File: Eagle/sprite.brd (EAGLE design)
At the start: 35 x 35 mm, 39 parts

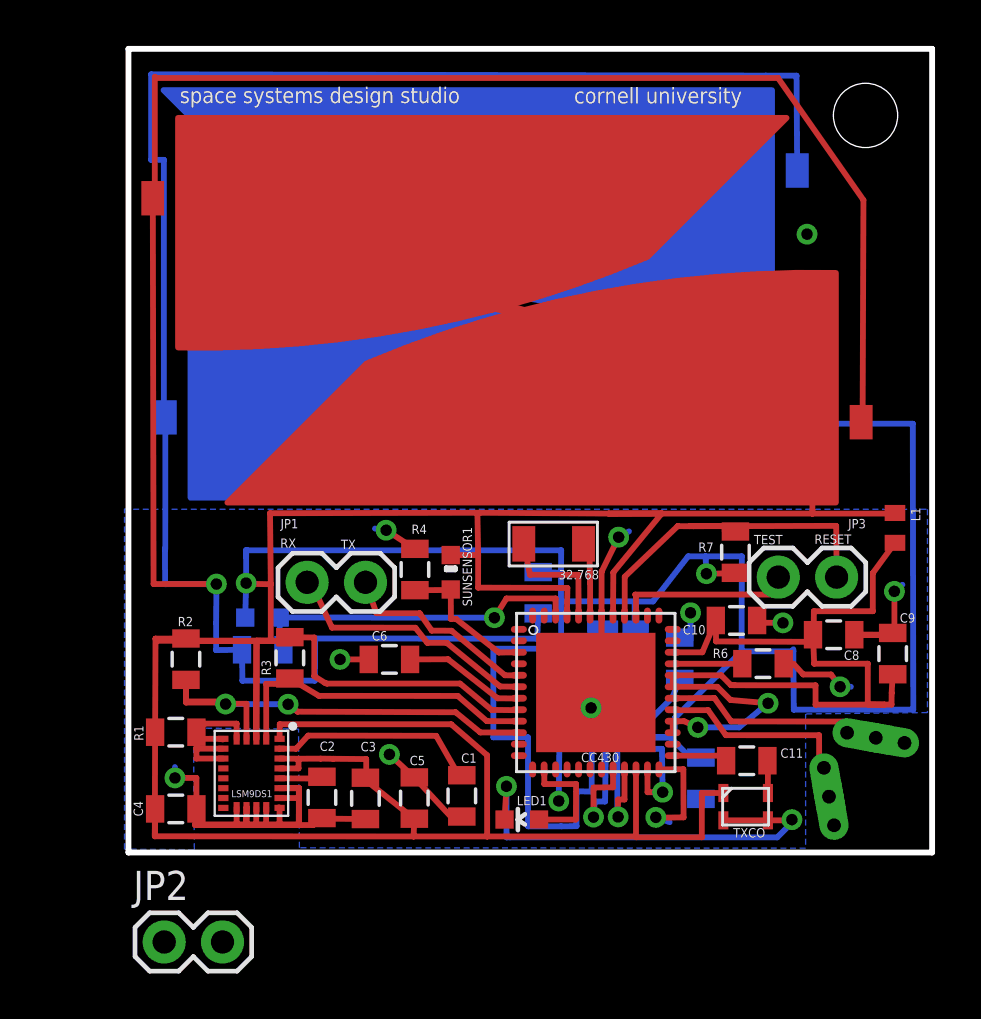
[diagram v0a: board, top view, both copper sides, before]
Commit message: Resized, still needs spacers
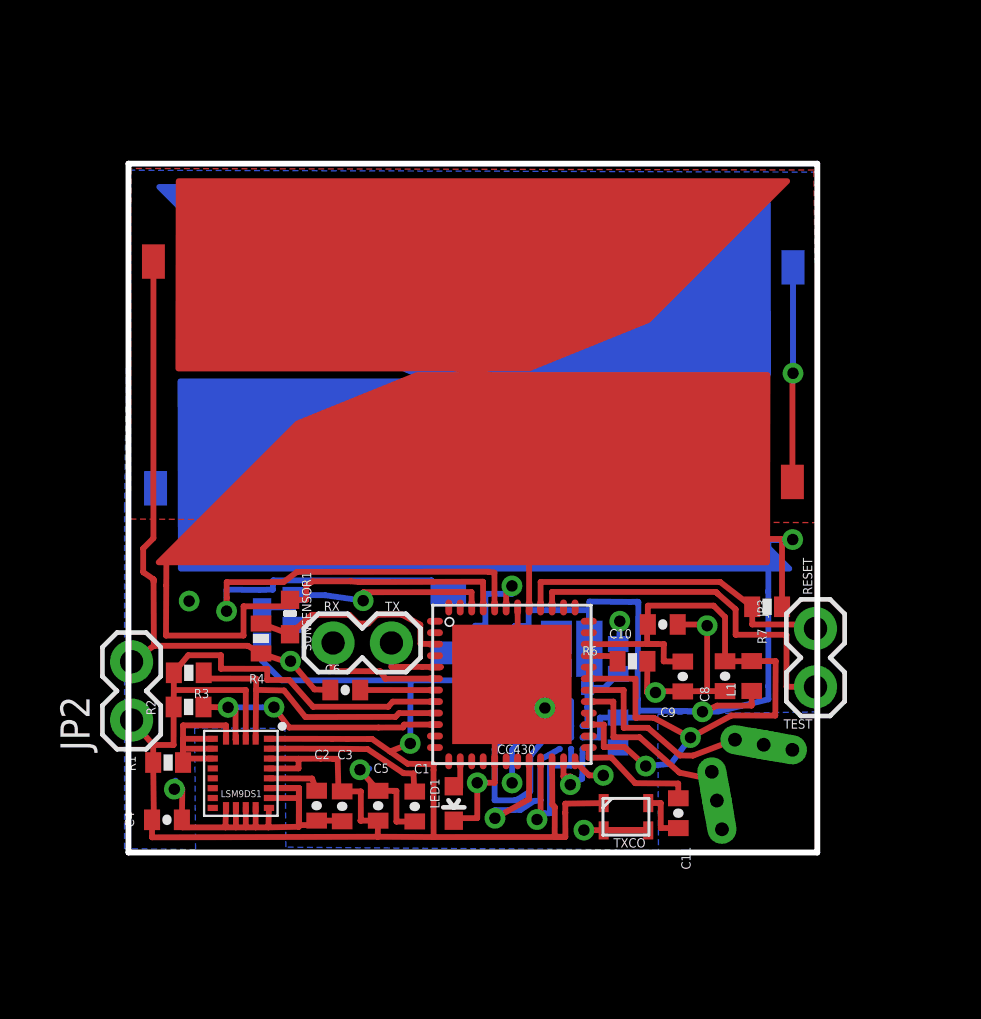
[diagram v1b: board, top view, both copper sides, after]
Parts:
- C1, C10, C11, C12, C2, C3, C4, C5, C6, C7, C8, C9: device SparkFun:0805 -> SparkFun-Passives:0402-CAP
- R1, R2, R3, R4, R5, R6, R7, R8: device SparkFun:0805 -> SparkFun-Passives:0402-RES
- moved JP2 9.77 mm to (0.14, 5.77), turned to 90 degrees
- moved C9 9.20 mm to (24.1, 7.67), turned to 270 degrees
- moved L1 8.97 mm to (27.1, 7.69), turned to 90 degrees
- moved R4 7.34 mm to (5.77, 9.32), turned to 90 degrees
- moved SUNSENSOR1 7.27 mm to (7.04, 10.3)
- moved 32KHZ 5.74 mm to (13.9, 10.00), flipped to the bottom, turned to 90 degrees
- moved R6 5.68 mm to (22.0, 8.33)
- moved TXCO 5.23 mm to (21.7, 1.56)
- moved C8 5.06 mm to (26.0, 7.68), turned to 270 degrees
- moved ANTENNA2 4.89 mm to (27.7, 4.69)
- moved ANTENNA1 4.89 mm to (25.6, 2.26)
- moved C7 4.59 mm to (16.0, 7.12)
- moved R3 4.45 mm to (2.63, 7.83), turned to 180 degrees
- moved TRISOL4 4.22 mm to (27.8, 29.0)
- moved C12 4.12 mm to (21.3, 5.23)
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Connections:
- removed net P3.4: CC430.17
- net GND: now also CC430.17
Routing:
- net COIL1: track 1132.3 -> 758.3 mm
- net GND: track 226.3 -> 109.0 mm, vias 12 -> 9
- net VCC: track 361.6 -> 331.4 mm, vias 2 -> 3
- net N$7: track 5.26 -> 25.8 mm, vias 0 -> 1
- net GUARD: track 44.1 -> 35.2 mm
- net SDA: track 21.1 -> 12.7 mm
- net TEST/SBWTCK: track 7.89 -> 15.8 mm
- net UART_RX: track 11.6 -> 5.86 mm
- net UART_TX: track 8.73 -> 3.45 mm
- net P2.5/A5: track 14.7 -> 10.7 mm
- net P3.7: track 5.18 -> 1.44 mm
- net P2.6: track 5.01 -> 1.48 mm
- net N$4: track 2.55 -> 5.48 mm
- net P2.0/A0: track 6.31 -> 9.23 mm
- net N$8: track 3.52 -> 6.08 mm, vias 0 -> 1
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- added copper zone on layer 1, net GND
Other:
- board size 35 x 35 mm -> 30 x 30 mm
- board text removed: "cornell university"
- board text removed: "space systems design studio"

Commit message: Diverted torque coils around IMU
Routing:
- net COIL1: track 758.3 -> 770.9 mm
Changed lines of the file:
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@@
 <layer number="21" name="tPlace" color="7" fill="1" visible="yes" active="yes"/>
 <layer number="22" name="bPlace" color="7" fill="1" visible="no" active="yes"/>
-<layer number="23" name="tOrigins" color="15" fill="1" visible="yes" active="yes"/>
+<layer number="23" name="tOrigins" color="15" fill="1" visible="no" active="yes"/>
 <layer number="24" name="bOrigins" color="15" fill="1" visible="no" active="yes"/>
 <layer number="25" name="tNames" color="7" fill="1" visible="no" active="yes"/>
@@
 <layer number="43" name="vRestrict" color="2" fill="10" visible="no" active="yes"/>
 <layer number="44" name="Drills" color="7" fill="1" visible="no" active="yes"/>
-<layer number="45" name="Holes" color="7" fill="1" visible="yes" active="yes"/>
+<layer number="45" name="Holes" color="7" fill="1" visible="no" active="yes"/>
 <layer number="46" name="Milling" color="3" fill="1" visible="no" active="yes"/>
 <layer number="47" name="Measures" color="7" fill="1" visible="no" active="yes"/>
@@
 <wire x1="21.331321875" y1="9.078028125" x2="21.376128125" y2="9.01871875" width="0.254" layer="16"/>
 <wire x1="21.376128125" y1="9.01871875" x2="21.39665625" y2="10.073121875" width="0.254" layer="16"/>
-<wire x1="14.0452125" y1="0.796771875" x2="2.96135625" y2="0.796771875" width="0.254" layer="15"/>
-<wire x1="2.96135625" y1="0.796771875" x2="2.96135625" y2="3.7204375" width="0.254" layer="15"/>
-<wire x1="2.96135625" y1="3.7204375" x2="1.502778125" y2="5.179015625" width="0.254" layer="15"/>
+<wire x1="14.0452125" y1="0.796771875" x2="0.6500375" y2="0.779525" width="0.254" layer="15"/>
+<wire x1="0.6500375" y1="0.779525" x2="0.6500375" y2="3.703190625" width="0.254" layer="15"/>
+<wire x1="0.6500375" y1="3.703190625" x2="1.502778125" y2="5.179015625" width="0.254" layer="15"/>
 <wire x1="1.502778125" y1="5.179015625" x2="1.502778125" y2="8.942859375" width="0.254" layer="15"/>
 <wire x1="1.502778125" y1="8.942859375" x2="0.76615" y2="9.642515625" width="0.254" layer="15"/>
@@
 <wire x1="20.52805625" y1="4.63108125" x2="13.523684375" y2="4.63108125" width="0.254" layer="15"/>
 <wire x1="13.523684375" y1="4.63108125" x2="13.523684375" y2="1.278603125" width="0.254" layer="15"/>
-<wire x1="13.523684375" y1="1.278603125" x2="3.683278125" y2="1.278603125" width="0.254" layer="15"/>
-<wire x1="3.683278125" y1="1.278603125" x2="3.6797875" y2="1.278603125" width="0.254" layer="15"/>
-<wire x1="3.683278125" y1="1.278603125" x2="3.683278125" y2="3.712134375" width="0.254" layer="15"/>
-<wire x1="3.683278125" y1="3.712134375" x2="2.043740625" y2="5.351671875" width="0.254" layer="15"/>
-<wire x1="2.043740625" y1="5.351671875" x2="2.043740625" y2="9.124634375" width="0.254" layer="15"/>
+<wire x1="13.523684375" y1="1.278603125" x2="1.185465625" y2="1.280303125" width="0.254" layer="15"/>
+<wire x1="1.185465625" y1="1.280303125" x2="3.6797875" y2="1.278603125" width="0.254" layer="15"/>
+<wire x1="1.185465625" y1="1.280303125" x2="1.185465625" y2="3.713834375" width="0.254" layer="15"/>
+<wire x1="1.185465625" y1="3.713834375" x2="2.0337625" y2="5.1620625" width="0.254" layer="15"/>
+<wire x1="2.0337625" y1="5.1620625" x2="2.043740625" y2="9.124634375" width="0.254" layer="15"/>
 <wire x1="2.043740625" y1="9.124634375" x2="1.276396875" y2="9.891978125" width="0.254" layer="15"/>
 <wire x1="1.276396875" y1="9.891978125" x2="1.276396875" y2="28.823284375" width="0.254" layer="15"/>
@@
 <wire x1="20.0016375" y1="5.10645625" x2="13.020675" y2="5.10645625" width="0.254" layer="15"/>
 <wire x1="13.020675" y1="5.10645625" x2="13.020675" y2="1.7901125" width="0.254" layer="15"/>
-<wire x1="13.020675" y1="1.7901125" x2="4.356575" y2="1.7901125" width="0.254" layer="15"/>
-<wire x1="4.356575" y1="1.7901125" x2="4.356578125" y2="3.728709375" width="0.254" layer="15"/>
-<wire x1="4.356578125" y1="3.728709375" x2="2.65175" y2="5.4335375" width="0.254" layer="15"/>
-<wire x1="2.65175" y1="5.4335375" x2="2.62709375" y2="9.314578125" width="0.254" layer="15"/>
+<wire x1="13.020675" y1="1.7901125" x2="6.711528125" y2="1.844990625" width="0.254" layer="15"/>
+<wire x1="6.711528125" y1="1.844990625" x2="6.68356875" y2="5.499759375" width="0.254" layer="15"/>
+<wire x1="6.68356875" y1="5.499759375" x2="2.605565625" y2="5.520140625" width="0.254" layer="15"/>
+<wire x1="2.605565625" y1="5.520140625" x2="2.62709375" y2="9.314578125" width="0.254" layer="15"/>
 <wire x1="2.62709375" y1="9.314578125" x2="1.8112" y2="10.130471875" width="0.254" layer="15"/>
 <wire x1="1.8112" y1="10.130471875" x2="1.8112" y2="28.349396875" width="0.254" layer="15"/>
@@
 <wire x1="11.464903125" y1="3.9649625" x2="12.50891875" y2="3.9649625" width="0.254" layer="15"/>
 <wire x1="12.50891875" y1="3.9649625" x2="12.50891875" y2="2.2906375" width="0.254" layer="15"/>
-<wire x1="12.50891875" y1="2.2906375" x2="4.9501625" y2="2.2906375" width="0.254" layer="15"/>
-<wire x1="4.9501625" y1="2.2906375" x2="4.9501625" y2="3.88310625" width="0.254" layer="15"/>
-<wire x1="4.9501625" y1="3.88310625" x2="3.214525" y2="5.61874375" width="0.254" layer="15"/>
-<wire x1="3.214525" y1="5.61874375" x2="3.214525" y2="10.379796875" width="0.254" layer="15"/>
+<wire x1="12.50891875" y1="2.2906375" x2="7.1924" y2="2.2906375" width="0.254" layer="15"/>
+<wire x1="7.1924" y1="2.2906375" x2="7.17803125" y2="7.13495625" width="0.254" layer="15"/>
+<wire x1="7.17803125" y1="7.13495625" x2="3.24326875" y2="7.131103125" width="0.254" layer="15"/>
+<wire x1="3.24326875" y1="7.131103125" x2="3.214525" y2="10.379796875" width="0.254" layer="15"/>
 <wire x1="3.214525" y1="10.379796875" x2="2.642496875" y2="10.951825" width="0.254" layer="15"/>
 <wire x1="2.642496875" y1="10.951825" x2="2.33168125" y2="11.262640625" width="0.254" layer="2"/>
@@
 <wire x1="11.4447875" y1="3.97566875" x2="12.497309375" y2="3.97566875" width="0.254" layer="2"/>
 <wire x1="12.497309375" y1="3.97566875" x2="12.497309375" y2="2.296875" width="0.254" layer="2"/>
-<wire x1="12.497309375" y1="2.296875" x2="4.949346875" y2="2.296875" width="0.254" layer="2"/>
-<wire x1="4.949346875" y1="2.296875" x2="4.949346875" y2="3.878165625" width="0.254" layer="2"/>
-<wire x1="4.949346875" y1="3.878165625" x2="2.640103125" y2="6.187409375" width="0.254" layer="2"/>
-<wire x1="2.640103125" y1="6.187409375" x2="2.640103125" y2="9.318675" width="0.254" layer="2"/>
+<wire x1="12.497309375" y1="2.296875" x2="7.202546875" y2="2.293490625" width="0.254" layer="2"/>
+<wire x1="7.202546875" y1="2.293490625" x2="7.15326875" y2="7.14310625" width="0.254" layer="2"/>
+<wire x1="7.15326875" y1="7.14310625" x2="2.62573125" y2="7.164975" width="0.254" layer="2"/>
+<wire x1="2.62573125" y1="7.164975" x2="2.640103125" y2="9.318675" width="0.254" layer="2"/>
 <wire x1="2.640103125" y1="9.318675" x2="1.81888125" y2="10.139896875" width="0.254" layer="2"/>
 <wire x1="1.81888125" y1="10.139896875" x2="1.81888125" y2="28.350465625" width="0.254" layer="2"/>
@@
 <wire x1="19.4828" y1="5.106703125" x2="13.018928125" y2="5.106703125" width="0.254" layer="2"/>
 <wire x1="13.018928125" y1="5.106703125" x2="13.018928125" y2="1.7922" width="0.254" layer="2"/>
-<wire x1="13.018928125" y1="1.7922" x2="4.358153125" y2="1.7922" width="0.254" layer="2"/>
-<wire x1="4.358153125" y1="1.7922" x2="4.358153125" y2="3.73108125" width="0.254" layer="2"/>
-<wire x1="4.358153125" y1="3.73108125" x2="2.0420625" y2="6.047171875" width="0.254" layer="2"/>
-<wire x1="2.0420625" y1="6.047171875" x2="2.0420625" y2="9.1243" width="0.254" layer="2"/>
+<wire x1="13.018928125" y1="1.7922" x2="6.703375" y2="1.8473" width="0.254" layer="2"/>
+<wire x1="6.703375" y1="1.8473" x2="6.681165625" y2="5.501021875" width="0.254" layer="2"/>
+<wire x1="6.681165625" y1="5.501021875" x2="2.01711875" y2="5.531640625" width="0.254" layer="2"/>
+<wire x1="2.01711875" y1="5.531640625" x2="2.0420625" y2="9.1243" width="0.254" layer="2"/>
 <wire x1="2.0420625" y1="9.1243" x2="1.27515625" y2="9.89120625" width="0.254" layer="2"/>
 <wire x1="1.27515625" y1="9.89120625" x2="1.27515625" y2="28.82504375" width="0.254" layer="2"/>
@@
 <wire x1="19.99936875" y1="4.633625" x2="13.52375" y2="4.633625" width="0.254" layer="2"/>
 <wire x1="13.52375" y1="4.633625" x2="13.52375" y2="1.280828125" width="0.254" layer="2"/>
-<wire x1="13.52375" y1="1.280828125" x2="3.679021875" y2="1.280828125" width="0.254" layer="2"/>
-<wire x1="3.679021875" y1="1.280828125" x2="3.679021875" y2="3.716196875" width="0.254" layer="2"/>
-<wire x1="3.679021875" y1="3.716196875" x2="1.500796875" y2="5.894421875" width="0.254" layer="2"/>
+<wire x1="13.52375" y1="1.280828125" x2="1.17445" y2="1.29080625" width="0.254" layer="2"/>
+<wire x1="1.17445" y1="1.29080625" x2="1.17445" y2="3.726175" width="0.254" layer="2"/>
+<wire x1="1.17445" y1="3.726175" x2="1.500796875" y2="5.894421875" width="0.254" layer="2"/>
 <wire x1="1.500796875" y1="5.894421875" x2="1.500796875" y2="8.9059375" width="0.254" layer="2"/>
 <wire x1="1.500796875" y1="8.9059375" x2="0.763715625" y2="9.64301875" width="0.254" layer="2"/>
